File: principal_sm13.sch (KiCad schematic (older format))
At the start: 3 parts

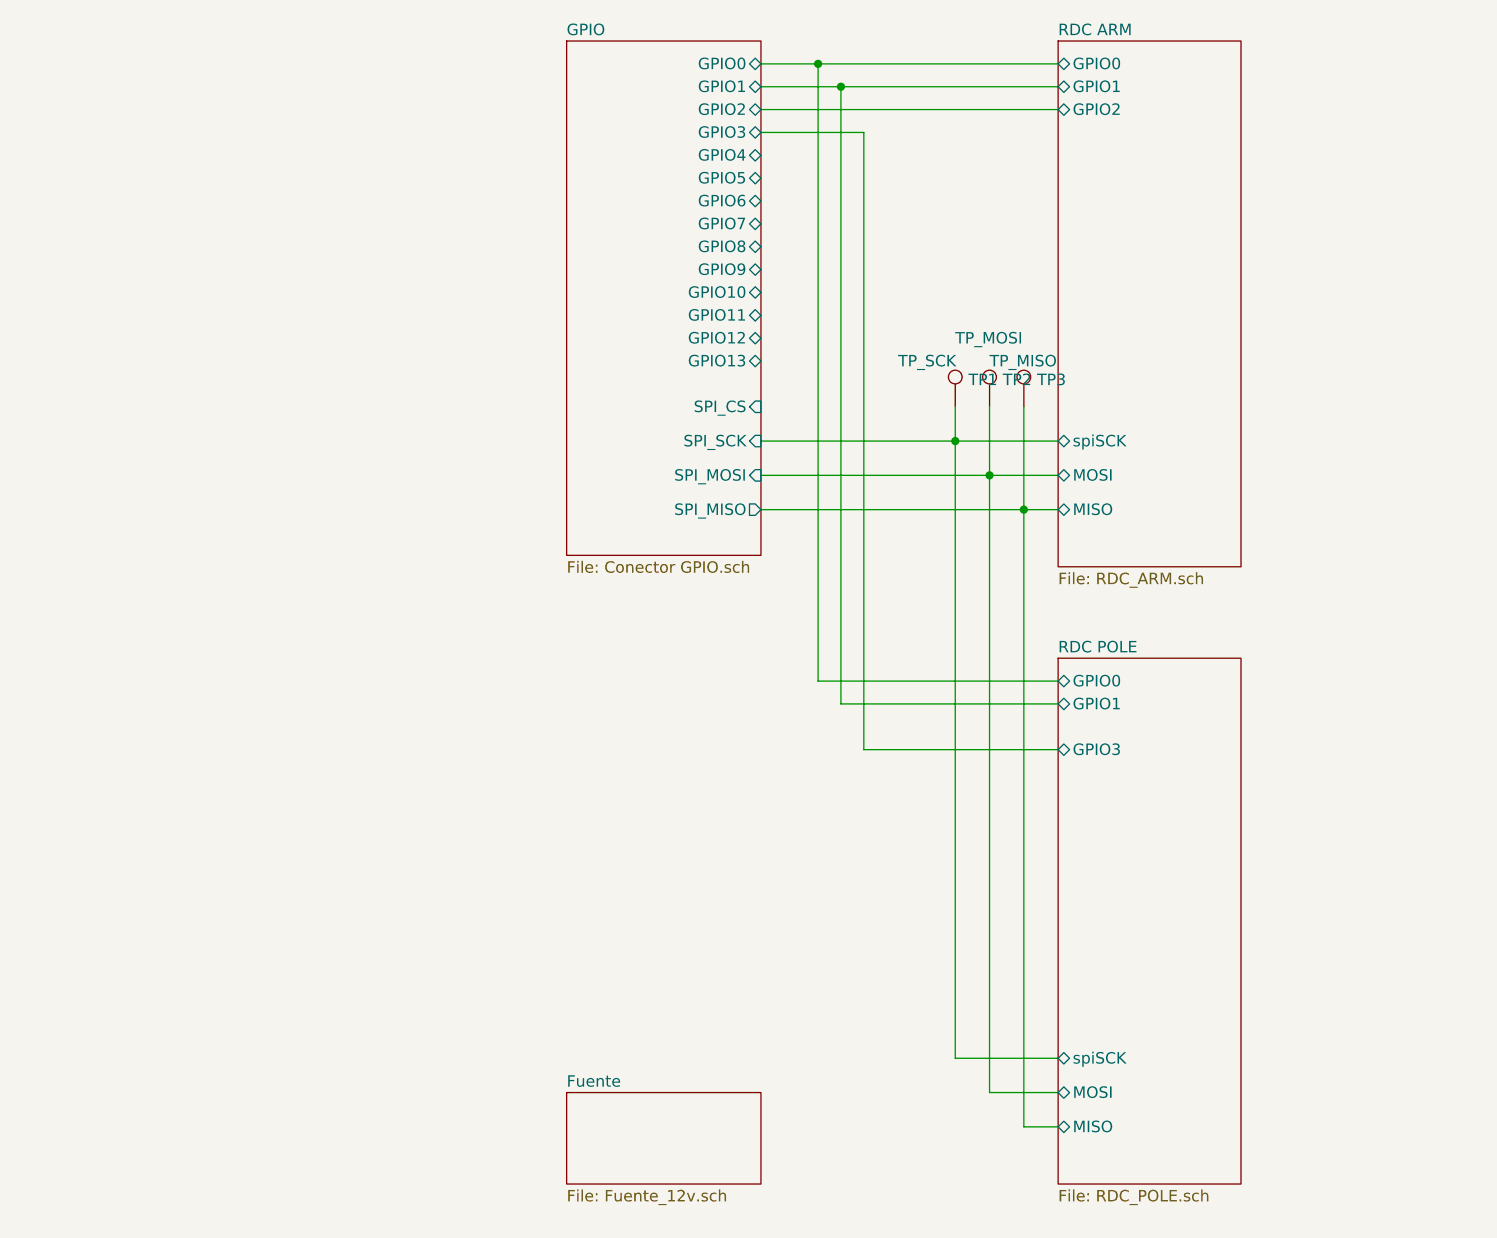
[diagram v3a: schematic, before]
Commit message: cambiados conectores, agregado conversor 3,3->TTL drivers
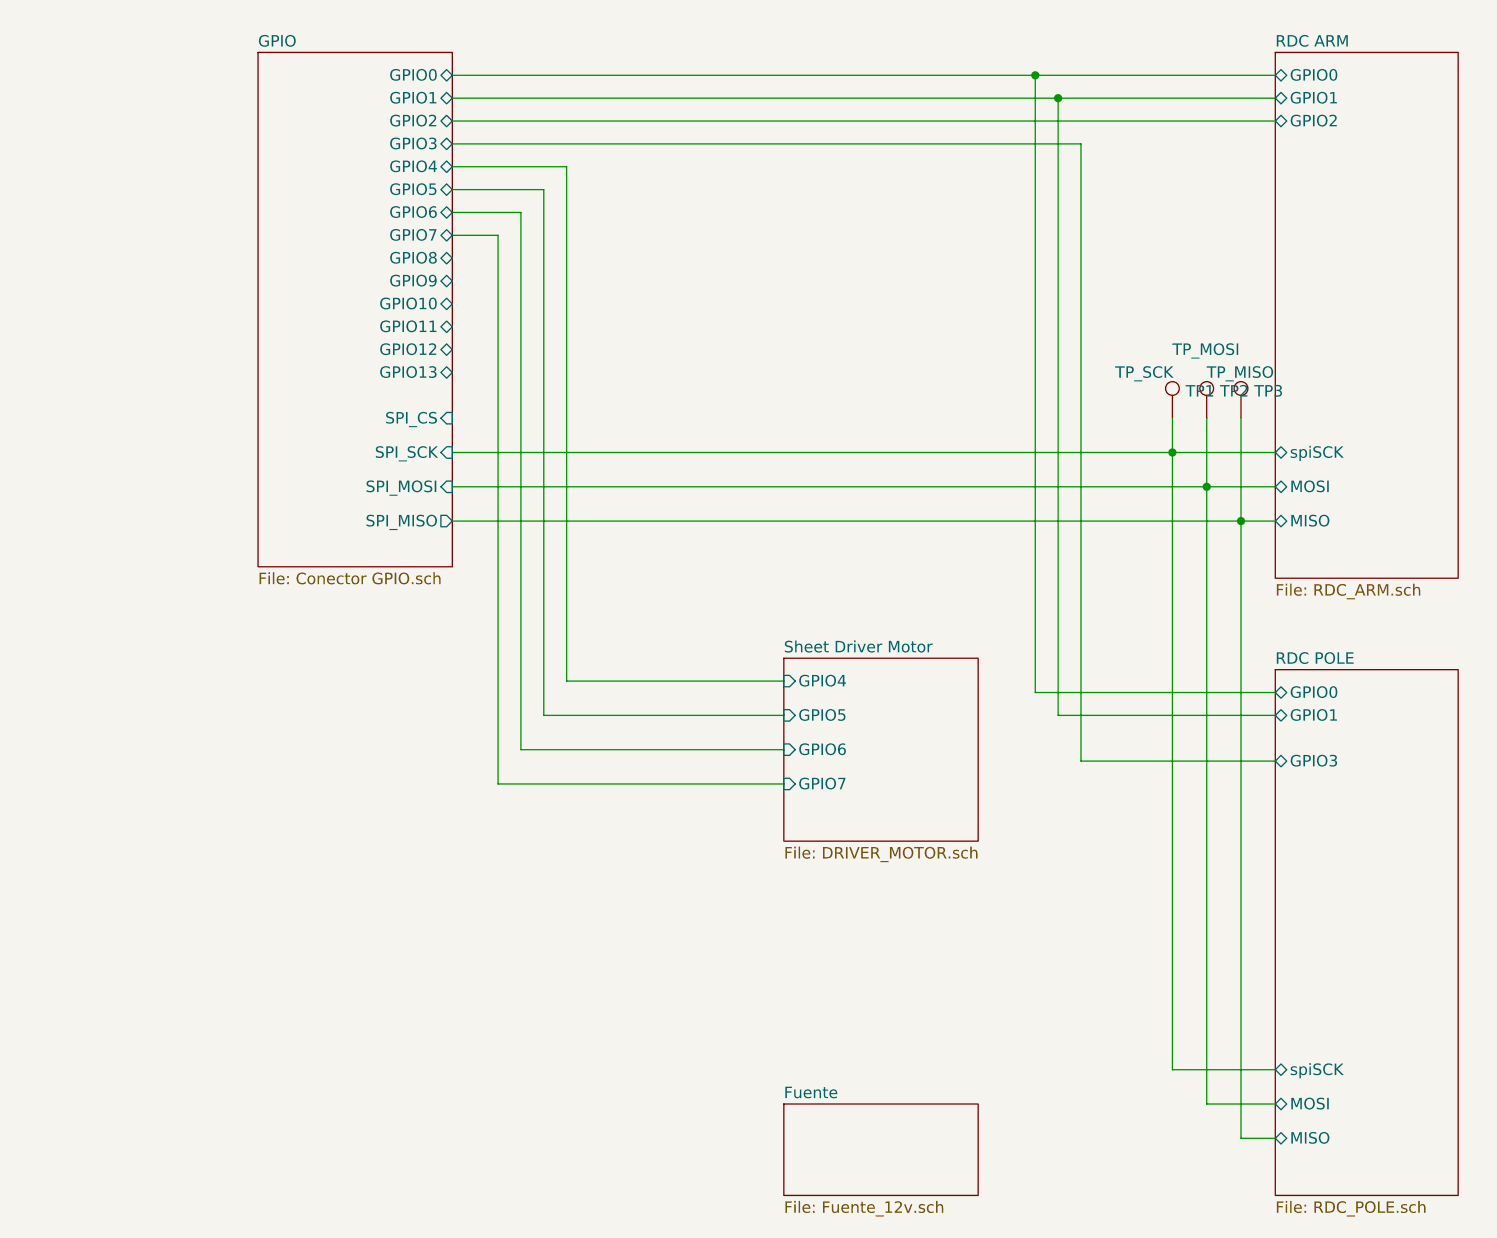
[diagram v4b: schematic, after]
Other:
- moved on the sheet: TP1, TP2, TP3
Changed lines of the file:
@@
 $Descr A4 11693 8268
 encoding utf-8
-Sheet 1 5
+Sheet 1 6
 Title "RDC"
 Date "2020-06-22"
@@
 $EndDescr
 $Sheet
-S 4200 950  850  2250
+S 2850 1000 850  2250
 U 5EF2A268
 F0 "GPIO" 50
 F1 "Conector GPIO.sch" 50
-F2 "GPIO0" B R 5050 1050 50
-F3 "GPIO2" B R 5050 1250 50
-F4 "GPIO4" B R 5050 1450 50
-F5 "GPIO6" B R 5050 1650 50
-F6 "GPIO8" B R 5050 1850 50
-F7 "GPIO10" B R 5050 2050 50
-F8 "GPIO12" B R 5050 2250 50
-F9 "GPIO1" B R 5050 1150 50
-F10 "GPIO3" B R 5050 1350 50
-F11 "GPIO5" B R 5050 1550 50
-F12 "GPIO7" B R 5050 1750 50
-F13 "GPIO9" B R 5050 1950 50
-F14 "GPIO11" B R 5050 2150 50
-F15 "GPIO13" B R 5050 2350 50
-F16 "SPI_MISO" O R 5050 3000 50
-F17 "SPI_MOSI" I R 5050 2850 50
-F18 "SPI_SCK" I R 5050 2700 50
-F19 "SPI_CS" I R 5050 2550 50
+F2 "GPIO0" B R 3700 1100 50
+F3 "GPIO2" B R 3700 1300 50
+F4 "GPIO4" B R 3700 1500 50
+F5 "GPIO6" B R 3700 1700 50
+F6 "GPIO8" B R 3700 1900 50
+F7 "GPIO10" B R 3700 2100 50
+F8 "GPIO12" B R 3700 2300 50
+F9 "GPIO1" B R 3700 1200 50
+F10 "GPIO3" B R 3700 1400 50
+F11 "GPIO5" B R 3700 1600 50
+F12 "GPIO7" B R 3700 1800 50
+F13 "GPIO9" B R 3700 2000 50
+F14 "GPIO11" B R 3700 2200 50
+F15 "GPIO13" B R 3700 2400 50
+F16 "SPI_MISO" O R 3700 3050 50
+F17 "SPI_MOSI" I R 3700 2900 50
+F18 "SPI_SCK" I R 3700 2750 50
+F19 "SPI_CS" I R 3700 2600 50
 $EndSheet
-Wire Wire Line
-	5050 1050 5300 1050
-Wire Wire Line
-	5050 1150 5400 1150
-Wire Wire Line
-	5050 2700 5900 2700
-Wire Wire Line
-	5050 2850 6050 2850
-Wire Wire Line
-	5050 1250 6350 1250
 $Sheet
-S 6350 950  800  2300
+S 7300 1000 800  2300
 U 5EF45E27
 F0 "RDC ARM" 50
 F1 "RDC_ARM.sch" 50
-F2 "MISO" B L 6350 3000 50
-F3 "MOSI" B L 6350 2850 50
-F4 "spiSCK" B L 6350 2700 50
-F5 "GPIO2" B L 6350 1250 50
-F6 "GPIO0" B L 6350 1050 50
-F7 "GPIO1" B L 6350 1150 50
+F2 "MISO" B L 7300 3050 50
+F3 "MOSI" B L 7300 2900 50
+F4 "spiSCK" B L 7300 2750 50
+F5 "GPIO2" B L 7300 1300 50
+F6 "GPIO0" B L 7300 1100 50
+F7 "GPIO1" B L 7300 1200 50
 $EndSheet
 Wire Wire Line
-	5050 3000 6200 3000
+	6850 2750 6850 5450
 Wire Wire Line
-	5900 2700 5900 5400
+	7000 2900 7000 5600
 Wire Wire Line
-	6050 2850 6050 5550
+	7150 3050 7150 5750
+Connection ~ 6850 2750
+Connection ~ 7000 2900
+Connection ~ 7150 3050
 Wire Wire Line
-	6200 3000 6200 5700
-Connection ~ 5900 2700
-Connection ~ 6050 2850
-Connection ~ 6200 3000
+	6850 2750 7300 2750
 Wire Wire Line
-	5900 2700 6350 2700
+	7000 2900 7300 2900
 Wire Wire Line
-	6050 2850 6350 2850
+	7150 3050 7300 3050
 Wire Wire Line
-	6200 3000 6350 3000
+	6850 5450 7300 5450
 Wire Wire Line
-	5900 5400 6350 5400
+	7000 5600 7300 5600
 Wire Wire Line
-	6050 5550 6350 5550
+	7150 5750 7300 5750
 Wire Wire Line
-	6200 5700 6350 5700
+	6250 1100 6250 3800
+Connection ~ 6250 1100
 Wire Wire Line
-	5300 1050 5300 3750
-Connection ~ 5300 1050
+	6250 1100 7300 1100
 Wire Wire Line
-	5300 1050 6350 1050
+	6250 3800 7300 3800
 Wire Wire Line
-	5300 3750 6350 3750
+	6350 1200 6350 3900
+Connection ~ 6350 1200
 Wire Wire Line
-	5400 1150 5400 3850
-Connection ~ 5400 1150
+	6350 1200 7300 1200
 Wire Wire Line
-	5400 1150 6350 1150
-Wire Wire Line
-	5400 3850 6350 3850
+	6350 3900 7300 3900
 $Sheet
-S 6350 3650 800  2300
+S 7300 3700 800  2300
 U 5F077C82
 F0 "RDC POLE" 50
 F1 "RDC_POLE.sch" 50
-F2 "MISO" B L 6350 5700 50
-F3 "MOSI" B L 6350 5550 50
-F4 "spiSCK" B L 6350 5400 50
-F5 "GPIO0" B L 6350 3750 50
-F6 "GPIO1" B L 6350 3850 50
-F7 "GPIO3" B L 6350 4050 50
+F2 "MISO" B L 7300 5750 50
+F3 "MOSI" B L 7300 5600 50
+F4 "spiSCK" B L 7300 5450 50
+F5 "GPIO0" B L 7300 3800 50
+F6 "GPIO1" B L 7300 3900 50
+F7 "GPIO3" B L 7300 4100 50
 $EndSheet
 Wire Wire Line
-	5050 1350 5500 1350
+	6450 1400 6450 4100
 Wire Wire Line
-	5500 1350 5500 4050
-Wire Wire Line
-	5500 4050 6350 4050
+	6450 4100 7300 4100
 $Sheet
-S 4200 5550 850  400
+S 5150 5600 850  400
 U 5EF34214
 F0 "Fuente" 50
@@
 L Connector:TestPoint TP1
 U 1 1 5F11CC37
-P 5900 2550
-F 0 "TP1" H 5958 2668 50  0000 L CNN
-F 1 "TP_SCK" H 5650 2750 50  0000 L CNN
-F 2 "TestPoint:TestPoint_THTPad_1.0x1.0mm_Drill0.5mm" H 6100 2550 50  0001 C CNN
-F 3 "~" H 6100 2550 50  0001 C CNN
-	1    5900 2550
+P 6850 2600
+F 0 "TP1" H 6908 2718 50  0000 L CNN
+F 1 "TP_SCK" H 6600 2800 50  0000 L CNN
+F 2 "TestPoint:TestPoint_THTPad_1.0x1.0mm_Drill0.5mm" H 7050 2600 50  0001 C CNN
+F 3 "~" H 7050 2600 50  0001 C CNN
+	1    6850 2600
 	1    0    0    -1
 $EndComp
@@
 L Connector:TestPoint TP2
 U 1 1 5F11D1E5
-P 6050 2550
-F 0 "TP2" H 6108 2668 50  0000 L CNN
-F 1 "TP_MOSI" H 5900 2850 50  0000 L CNN
-F 2 "TestPoint:TestPoint_THTPad_1.0x1.0mm_Drill0.5mm" H 6250 2550 50  0001 C CNN
-F 3 "~" H 6250 2550 50  0001 C CNN
-	1    6050 2550
+P 7000 2600
+F 0 "TP2" H 7058 2718 50  0000 L CNN
+F 1 "TP_MOSI" H 6850 2900 50  0000 L CNN
+F 2 "TestPoint:TestPoint_THTPad_1.0x1.0mm_Drill0.5mm" H 7200 2600 50  0001 C CNN
+F 3 "~" H 7200 2600 50  0001 C CNN
+	1    7000 2600
 	1    0    0    -1
 $EndComp
@@
 L Connector:TestPoint TP3
 U 1 1 5F11D4A3
-P 6200 2550
-F 0 "TP3" H 6258 2668 50  0000 L CNN
-F 1 "TP_MISO" H 6050 2750 50  0000 L CNN
-F 2 "TestPoint:TestPoint_THTPad_1.0x1.0mm_Drill0.5mm" H 6400 2550 50  0001 C CNN
-F 3 "~" H 6400 2550 50  0001 C CNN
-	1    6200 2550
+P 7150 2600
+F 0 "TP3" H 7208 2718 50  0000 L CNN
+F 1 "TP_MISO" H 7000 2800 50  0000 L CNN
+F 2 "TestPoint:TestPoint_THTPad_1.0x1.0mm_Drill0.5mm" H 7350 2600 50  0001 C CNN
+F 3 "~" H 7350 2600 50  0001 C CNN
+	1    7150 2600
 	1    0    0    -1
 $EndComp
 Wire Wire Line
-	5900 2550 5900 2700
+	6850 2600 6850 2750
 Wire Wire Line
-	6050 2550 6050 2850
+	7000 2600 7000 2900
 Wire Wire Line
-	6200 2550 6200 3000
+	7150 2600 7150 3050
+$Sheet
+S 5150 3650 850  800
+U 5F0E7624
+F0 "Sheet Driver Motor" 50
+F1 "DRIVER_MOTOR.sch" 50
+F2 "GPIO4" I L 5150 3750 50
+F3 "GPIO5" I L 5150 3900 50
+F4 "GPIO6" I L 5150 4050 50
+F5 "GPIO7" I L 5150 4200 50
+$EndSheet
+Wire Wire Line
+	3700 1500 4200 1500
+Wire Wire Line
+	4200 1500 4200 3750
+Wire Wire Line
+	4200 3750 5150 3750
+Wire Wire Line
+	3700 1600 4100 1600
+Wire Wire Line
+	4100 1600 4100 3900
+Wire Wire Line
+	4100 3900 5150 3900
+Wire Wire Line
+	4000 1700 4000 4050
+Wire Wire Line
+	3700 2750 6850 2750
+Wire Wire Line
+	3700 2900 7000 2900
+Wire Wire Line
+	3700 3050 7150 3050
+Wire Wire Line
+	4000 4050 5150 4050
+Wire Wire Line
+	3700 1700 4000 1700
+Wire Wire Line
+	3700 1100 6250 1100
+Wire Wire Line
+	3700 1200 6350 1200
+Wire Wire Line
+	3700 1300 7300 1300
+Wire Wire Line
+	3700 1400 6450 1400
+Wire Wire Line
+	3700 1800 3900 1800
+Wire Wire Line
+	3900 1800 3900 4200
+Wire Wire Line
+	3900 4200 5150 4200
 $EndSCHEMATC

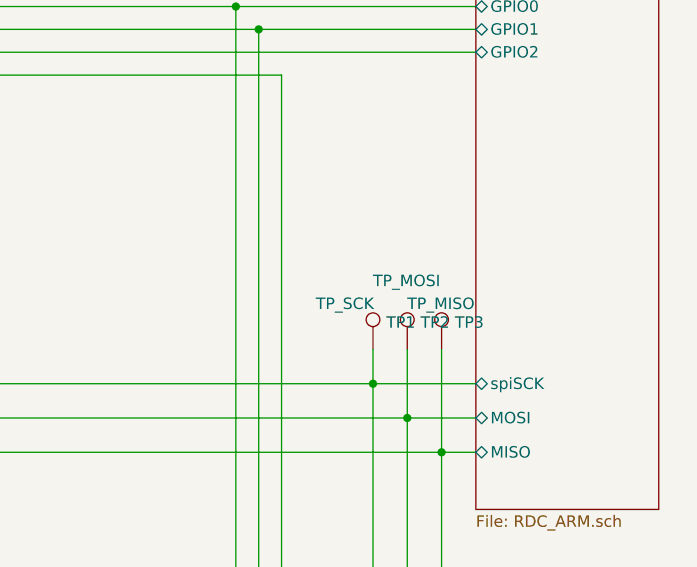
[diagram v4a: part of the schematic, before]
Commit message: outline reducido, para revision por peers
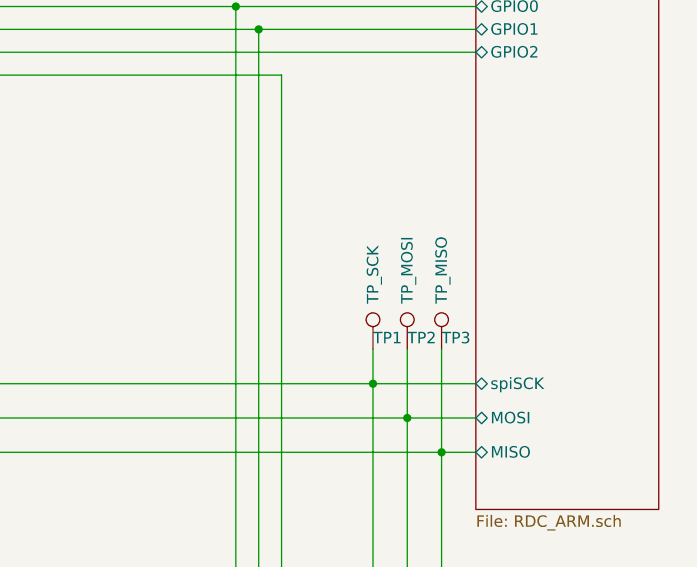
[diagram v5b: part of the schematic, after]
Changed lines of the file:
@@
 U 1 1 5F11CC37
 P 6850 2600
-F 0 "TP1" H 6908 2718 50  0000 L CNN
-F 1 "TP_SCK" H 6600 2800 50  0000 L CNN
+F 0 "TP1" H 6850 2650 50  0000 L CNN
+F 1 "TP_SCK" V 6850 2800 50  0000 L CNN
 F 2 "TestPoint:TestPoint_THTPad_1.0x1.0mm_Drill0.5mm" H 7050 2600 50  0001 C CNN
 F 3 "~" H 7050 2600 50  0001 C CNN
@@
 U 1 1 5F11D1E5
 P 7000 2600
-F 0 "TP2" H 7058 2718 50  0000 L CNN
-F 1 "TP_MOSI" H 6850 2900 50  0000 L CNN
+F 0 "TP2" H 7000 2650 50  0000 L CNN
+F 1 "TP_MOSI" V 7000 2800 50  0000 L CNN
 F 2 "TestPoint:TestPoint_THTPad_1.0x1.0mm_Drill0.5mm" H 7200 2600 50  0001 C CNN
 F 3 "~" H 7200 2600 50  0001 C CNN
@@
 U 1 1 5F11D4A3
 P 7150 2600
-F 0 "TP3" H 7208 2718 50  0000 L CNN
-F 1 "TP_MISO" H 7000 2800 50  0000 L CNN
+F 0 "TP3" H 7150 2650 50  0000 L CNN
+F 1 "TP_MISO" V 7150 2800 50  0000 L CNN
 F 2 "TestPoint:TestPoint_THTPad_1.0x1.0mm_Drill0.5mm" H 7350 2600 50  0001 C CNN
 F 3 "~" H 7350 2600 50  0001 C CNN

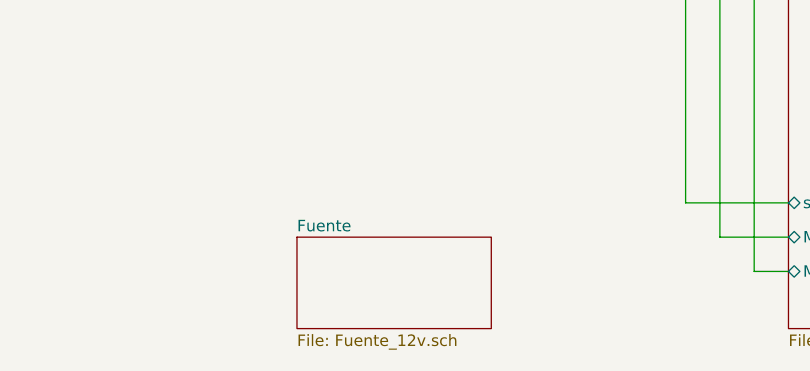
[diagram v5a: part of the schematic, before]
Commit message: eliminado regulador 12v, alimentar CIAA con 12v directamente
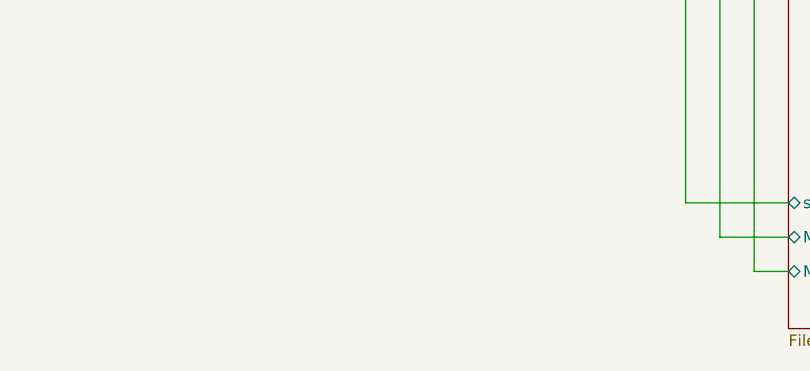
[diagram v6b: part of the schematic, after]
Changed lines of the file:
@@
 $Descr A4 11693 8268
 encoding utf-8
-Sheet 1 6
+Sheet 1 5
 Title "RDC"
 Date "2020-06-22"
@@
 Wire Wire Line
 	6450 4100 7300 4100
-$Sheet
-S 5150 5600 850  400
-U 5EF34214
-F0 "Fuente" 50
-F1 "Fuente_12v.sch" 50
-$EndSheet
 $Comp
 L Connector:TestPoint TP1

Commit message: cambiados capacitores electroliticos por tantalio (unpolarized). Agrandado footprint test pads, generado BOM, 35 vias
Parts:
- TP1, TP2, TP3: footprint TestPoint:TestPoint_THTPad_1.0x1.0mm_Drill0.5mm -> TestPoint:TestPoint_THTPad_1.5x1.5mm_Drill0.7mm
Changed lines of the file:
@@
 F 0 "TP1" H 6850 2650 50  0000 L CNN
 F 1 "TP_SCK" V 6850 2800 50  0000 L CNN
-F 2 "TestPoint:TestPoint_THTPad_1.0x1.0mm_Drill0.5mm" H 7050 2600 50  0001 C CNN
+F 2 "TestPoint:TestPoint_THTPad_1.5x1.5mm_Drill0.7mm" H 7050 2600 50  0001 C CNN
 F 3 "~" H 7050 2600 50  0001 C CNN
 	1    6850 2600
@@
 F 0 "TP2" H 7000 2650 50  0000 L CNN
 F 1 "TP_MOSI" V 7000 2800 50  0000 L CNN
-F 2 "TestPoint:TestPoint_THTPad_1.0x1.0mm_Drill0.5mm" H 7200 2600 50  0001 C CNN
+F 2 "TestPoint:TestPoint_THTPad_1.5x1.5mm_Drill0.7mm" H 7200 2600 50  0001 C CNN
 F 3 "~" H 7200 2600 50  0001 C CNN
 	1    7000 2600
@@
 F 0 "TP3" H 7150 2650 50  0000 L CNN
 F 1 "TP_MISO" V 7150 2800 50  0000 L CNN
-F 2 "TestPoint:TestPoint_THTPad_1.0x1.0mm_Drill0.5mm" H 7350 2600 50  0001 C CNN
+F 2 "TestPoint:TestPoint_THTPad_1.5x1.5mm_Drill0.7mm" H 7350 2600 50  0001 C CNN
 F 3 "~" H 7350 2600 50  0001 C CNN
 	1    7150 2600

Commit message: agrandados pads de test points
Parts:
- TP1, TP2, TP3: footprint TestPoint:TestPoint_THTPad_1.5x1.5mm_Drill0.7mm -> TestPoint:TestPoint_reducido
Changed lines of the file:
@@
 F 0 "TP1" H 6850 2650 50  0000 L CNN
 F 1 "TP_SCK" V 6850 2800 50  0000 L CNN
-F 2 "TestPoint:TestPoint_THTPad_1.5x1.5mm_Drill0.7mm" H 7050 2600 50  0001 C CNN
+F 2 "TestPoint:TestPoint_reducido" H 7050 2600 50  0001 C CNN
 F 3 "~" H 7050 2600 50  0001 C CNN
 	1    6850 2600
@@
 F 0 "TP2" H 7000 2650 50  0000 L CNN
 F 1 "TP_MOSI" V 7000 2800 50  0000 L CNN
-F 2 "TestPoint:TestPoint_THTPad_1.5x1.5mm_Drill0.7mm" H 7200 2600 50  0001 C CNN
+F 2 "TestPoint:TestPoint_reducido" H 7200 2600 50  0001 C CNN
 F 3 "~" H 7200 2600 50  0001 C CNN
 	1    7000 2600
@@
 F 0 "TP3" H 7150 2650 50  0000 L CNN
 F 1 "TP_MISO" V 7150 2800 50  0000 L CNN
-F 2 "TestPoint:TestPoint_THTPad_1.5x1.5mm_Drill0.7mm" H 7350 2600 50  0001 C CNN
+F 2 "TestPoint:TestPoint_reducido" H 7350 2600 50  0001 C CNN
 F 3 "~" H 7350 2600 50  0001 C CNN
 	1    7150 2600
